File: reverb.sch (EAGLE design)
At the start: 70 parts, among them IC2 TL074, IC2_EQ1 NE5532, IC4_DRV_RCVR TL072, T1 2N3904

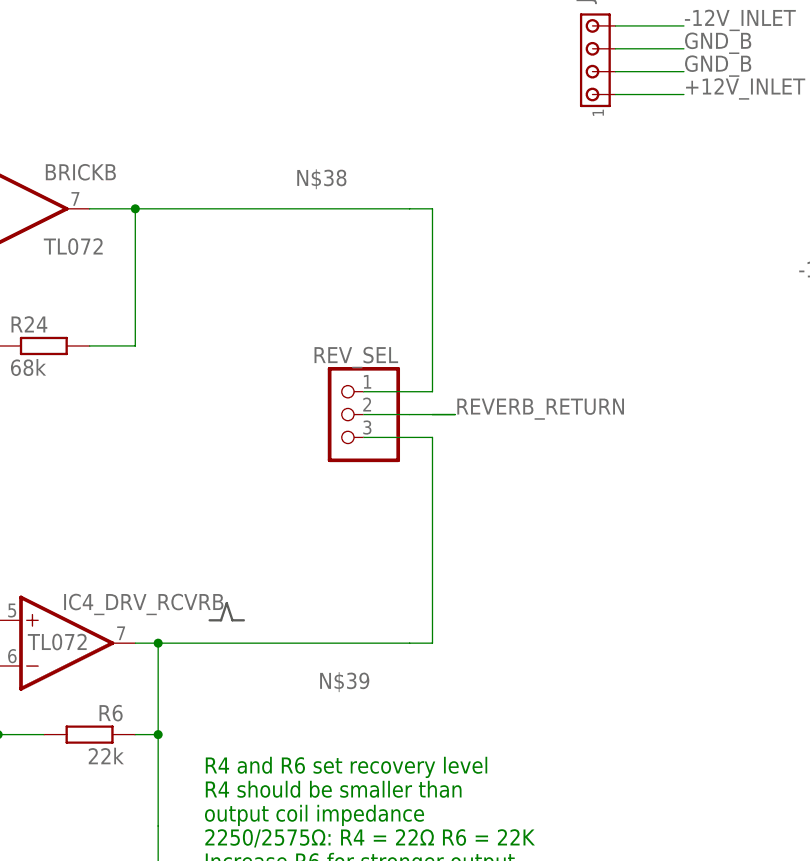
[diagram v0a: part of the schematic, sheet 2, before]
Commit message: fixed multiple power busses, ditched selection jumpers, layed out more board
selection jumpers: we're just gonna ditch part of the schematic anyways
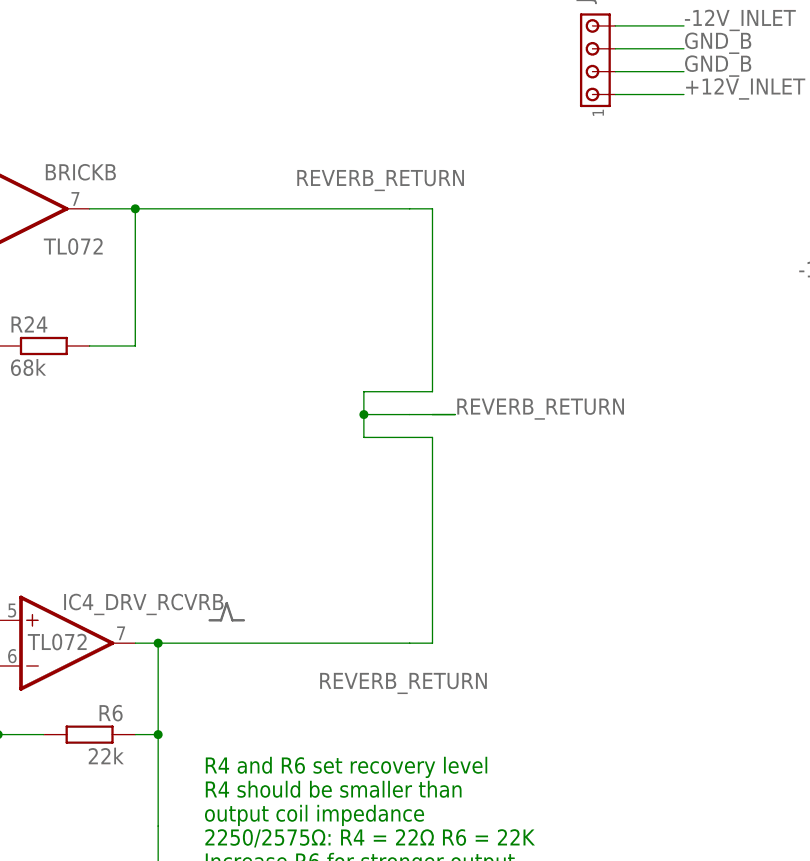
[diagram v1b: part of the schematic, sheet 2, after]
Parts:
- removed REV_SEL: (no value), pinhead:PINHD-1X3
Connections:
- removed net -12V: C11.1, C16.2
- removed net N$38: BRICKB.OUT, R24.2, REV_SEL.1
- removed net N$39: C9.2, IC4_DRV_RCVRB.OUT, R6.1, REV_SEL.3
- net +12V: no longer C10.2, C5.2
- net +12V_B: now also C10.2, C5.2
- net -12V_B: now also C11.1, C16.2
- net REVERB_RETURN: now also BRICKB.OUT, C9.2, IC4_DRV_RCVRB.OUT, R24.2, R6.1; no longer REV_SEL.2
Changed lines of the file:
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@@
 <part name="CV_IN" library="pinhead" deviceset="PINHD-1X2" device=""/>
 <part name="J1" library="con-amp" deviceset="MTA04-156" device=""/>
-<part name="REV_SEL" library="pinhead" deviceset="PINHD-1X3" device=""/>
 </parts>
 <sheets>
@@
 <label x="68.58" y="127" size="1.778" layer="95"/>
 </segment>
+<segment>
+<pinref part="C10" gate="G$1" pin="2"/>
+<wire x1="38.1" y1="88.9" x2="38.1" y2="86.36" width="0.1524" layer="91"/>
+<label x="38.1" y="88.9" size="1.778" layer="95"/>
+<pinref part="C5" gate="G$1" pin="2"/>
+<wire x1="50.8" y1="86.36" x2="38.1" y2="86.36" width="0.1524" layer="91"/>
+<junction x="38.1" y="86.36"/>
+</segment>
 </net>
 <net name="GND_B" class="2">
@@
 <label x="185.42" y="127" size="1.778" layer="95"/>
 </segment>
-</net>
-<net name="+12V" class="1">
-<segment>
-<pinref part="C10" gate="G$1" pin="2"/>
-<wire x1="38.1" y1="88.9" x2="38.1" y2="86.36" width="0.1524" layer="91"/>
-<label x="38.1" y="88.9" size="1.778" layer="95"/>
-<pinref part="C5" gate="G$1" pin="2"/>
-<wire x1="50.8" y1="86.36" x2="38.1" y2="86.36" width="0.1524" layer="91"/>
-<junction x="38.1" y="86.36"/>
-</segment>
-</net>
-<net name="-12V" class="1">
 <segment>
 <pinref part="C11" gate="G$1" pin="1"/>
@@
 <instance part="R2" gate="G$1" x="33.02" y="55.88"/>
 <instance part="J1" gate="G$3" x="205.74" y="157.48" rot="R90"/>
-<instance part="REV_SEL" gate="A" x="177.8" y="121.92" rot="MR0"/>
 </instances>
 <busses>
@@
 <label x="190.5" y="121.92" size="1.778" layer="95"/>
 <wire x1="190.5" y1="121.92" x2="187.96" y2="121.92" width="0.1524" layer="91"/>
-<pinref part="REV_SEL" gate="A" pin="2"/>
 <wire x1="187.96" y1="121.92" x2="185.42" y2="121.92" width="0.1524" layer="91"/>
 <wire x1="185.42" y1="121.92" x2="180.34" y2="121.92" width="0.1524" layer="91"/>
+<pinref part="BRICK" gate="B" pin="OUT"/>
+<wire x1="149.86" y1="144.78" x2="154.94" y2="144.78" width="0.1524" layer="91"/>
+<wire x1="154.94" y1="144.78" x2="185.42" y2="144.78" width="0.1524" layer="91"/>
+<pinref part="R24" gate="G$1" pin="2"/>
+<wire x1="149.86" y1="129.54" x2="154.94" y2="129.54" width="0.1524" layer="91"/>
+<wire x1="154.94" y1="129.54" x2="154.94" y2="144.78" width="0.1524" layer="91"/>
+<junction x="154.94" y="144.78"/>
+<label x="172.72" y="147.32" size="1.778" layer="95"/>
+<wire x1="185.42" y1="144.78" x2="187.96" y2="144.78" width="0.1524" layer="91"/>
+<wire x1="187.96" y1="144.78" x2="187.96" y2="124.46" width="0.1524" layer="91"/>
+<wire x1="187.96" y1="124.46" x2="180.34" y2="124.46" width="0.1524" layer="91"/>
+<wire x1="180.34" y1="124.46" x2="180.34" y2="121.92" width="0.1524" layer="91"/>
+<pinref part="R6" gate="G$1" pin="1"/>
+<wire x1="154.94" y1="86.36" x2="157.48" y2="86.36" width="0.1524" layer="91"/>
+<wire x1="157.48" y1="76.2" x2="157.48" y2="86.36" width="0.1524" layer="91"/>
+<wire x1="157.48" y1="63.5" x2="157.48" y2="76.2" width="0.1524" layer="91"/>
+<pinref part="C9" gate="G$1" pin="2"/>
+<wire x1="154.94" y1="63.5" x2="157.48" y2="63.5" width="0.1524" layer="91"/>
+<pinref part="IC4_DRV_RCVR" gate="B" pin="OUT"/>
+<wire x1="154.94" y1="96.52" x2="157.48" y2="96.52" width="0.1524" layer="91"/>
+<wire x1="157.48" y1="96.52" x2="185.42" y2="96.52" width="0.1524" layer="91"/>
+<wire x1="157.48" y1="86.36" x2="157.48" y2="96.52" width="0.1524" layer="91"/>
+<junction x="157.48" y="86.36"/>
+<junction x="157.48" y="96.52"/>
+<label x="175.26" y="91.44" size="1.778" layer="95"/>
+<wire x1="180.34" y1="119.38" x2="187.96" y2="119.38" width="0.1524" layer="91"/>
+<wire x1="187.96" y1="119.38" x2="187.96" y2="96.52" width="0.1524" layer="91"/>
+<wire x1="187.96" y1="96.52" x2="185.42" y2="96.52" width="0.1524" layer="91"/>
+<wire x1="180.34" y1="119.38" x2="180.34" y2="121.92" width="0.1524" layer="91"/>
+<junction x="180.34" y="121.92"/>
 </segment>
 </net>
@@
 </segment>
 </net>
-<net name="N$38" class="0">
-<segment>
-<pinref part="BRICK" gate="B" pin="OUT"/>
-<wire x1="149.86" y1="144.78" x2="154.94" y2="144.78" width="0.1524" layer="91"/>
-<wire x1="154.94" y1="144.78" x2="185.42" y2="144.78" width="0.1524" layer="91"/>
-<pinref part="R24" gate="G$1" pin="2"/>
-<wire x1="149.86" y1="129.54" x2="154.94" y2="129.54" width="0.1524" layer="91"/>
-<wire x1="154.94" y1="129.54" x2="154.94" y2="144.78" width="0.1524" layer="91"/>
-<junction x="154.94" y="144.78"/>
-<label x="172.72" y="147.32" size="1.778" layer="95"/>
-<wire x1="185.42" y1="144.78" x2="187.96" y2="144.78" width="0.1524" layer="91"/>
-<wire x1="187.96" y1="144.78" x2="187.96" y2="124.46" width="0.1524" layer="91"/>
-<pinref part="REV_SEL" gate="A" pin="1"/>
-<wire x1="187.96" y1="124.46" x2="180.34" y2="124.46" width="0.1524" layer="91"/>
-</segment>
-</net>
-<net name="N$39" class="0">
-<segment>
-<pinref part="R6" gate="G$1" pin="1"/>
-<wire x1="154.94" y1="86.36" x2="157.48" y2="86.36" width="0.1524" layer="91"/>
-<wire x1="157.48" y1="76.2" x2="157.48" y2="86.36" width="0.1524" layer="91"/>
-<wire x1="157.48" y1="63.5" x2="157.48" y2="76.2" width="0.1524" layer="91"/>
-<pinref part="C9" gate="G$1" pin="2"/>
-<wire x1="154.94" y1="63.5" x2="157.48" y2="63.5" width="0.1524" layer="91"/>
-<pinref part="IC4_DRV_RCVR" gate="B" pin="OUT"/>
-<wire x1="154.94" y1="96.52" x2="157.48" y2="96.52" width="0.1524" layer="91"/>
-<wire x1="157.48" y1="96.52" x2="185.42" y2="96.52" width="0.1524" layer="91"/>
-<wire x1="157.48" y1="86.36" x2="157.48" y2="96.52" width="0.1524" layer="91"/>
-<junction x="157.48" y="86.36"/>
-<junction x="157.48" y="96.52"/>
-<label x="175.26" y="91.44" size="1.778" layer="95"/>
-<pinref part="REV_SEL" gate="A" pin="3"/>
-<wire x1="180.34" y1="119.38" x2="187.96" y2="119.38" width="0.1524" layer="91"/>
-<wire x1="187.96" y1="119.38" x2="187.96" y2="96.52" width="0.1524" layer="91"/>
-<wire x1="187.96" y1="96.52" x2="185.42" y2="96.52" width="0.1524" layer="91"/>
-</segment>
-</net>

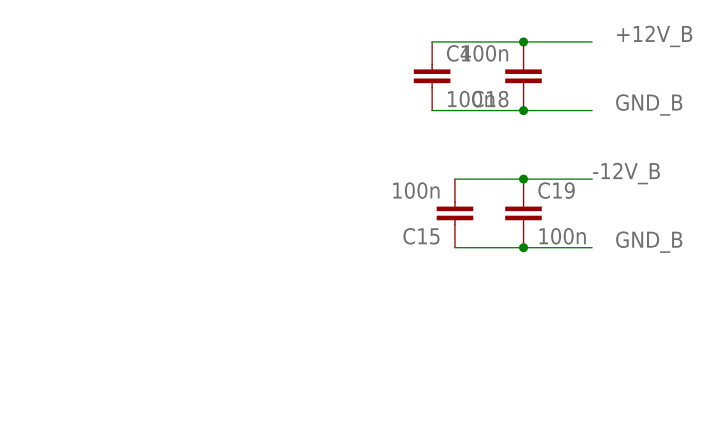
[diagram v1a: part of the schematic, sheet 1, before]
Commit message: everything should be on the board, just need to move it around
gonna ditch brick section soon, detached it
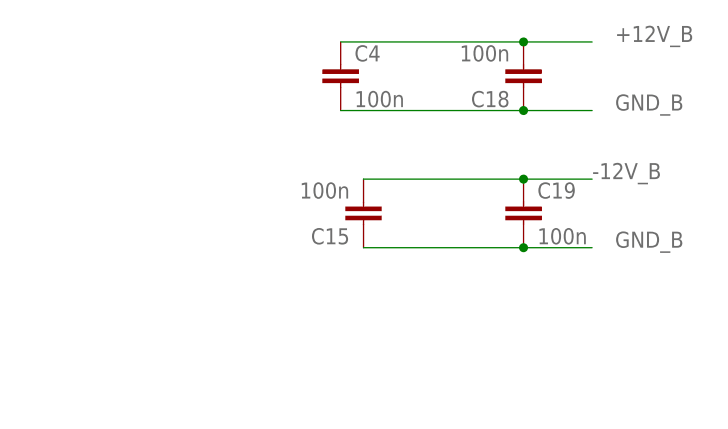
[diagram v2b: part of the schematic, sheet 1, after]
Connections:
- new net BRICKREVERB_SEND: R22.1
- new net BRICK_REVERB_RETURN: BRICKB.OUT, R24.2
- net REVERB_RETURN: no longer BRICKB.OUT, R24.2
- net REVERB_SEND: no longer R22.1
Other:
- moved on the sheet: C15, C4
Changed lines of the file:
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@@
 <instance part="FRAME2" gate="G$2" x="162.56" y="0"/>
 <instance part="IC4_DRV_RCVR" gate="P" x="170.18" y="81.28"/>
-<instance part="C4" gate="G$1" x="167.64" y="139.7"/>
-<instance part="C15" gate="G$1" x="170.18" y="121.92" rot="R180"/>
+<instance part="C4" gate="G$1" x="157.48" y="139.7"/>
+<instance part="C15" gate="G$1" x="160.02" y="121.92" rot="R180"/>
 <instance part="C14" gate="G$1" x="81.28" y="124.46"/>
 <instance part="C17" gate="G$1" x="81.28" y="109.22"/>
@@
 <label x="187.96" y="142.24" size="1.778" layer="95"/>
 <pinref part="C18" gate="G$1" pin="2"/>
-<wire x1="177.8" y1="142.24" x2="167.64" y2="142.24" width="0.1524" layer="91"/>
+<wire x1="177.8" y1="142.24" x2="157.48" y2="142.24" width="0.1524" layer="91"/>
 <junction x="177.8" y="142.24"/>
 </segment>
@@
 <label x="187.96" y="134.62" size="1.778" layer="95"/>
 <pinref part="C18" gate="G$1" pin="1"/>
-<wire x1="177.8" y1="134.62" x2="167.64" y2="134.62" width="0.1524" layer="91"/>
+<wire x1="177.8" y1="134.62" x2="157.48" y2="134.62" width="0.1524" layer="91"/>
 <junction x="177.8" y="134.62"/>
 </segment>
@@
 <label x="187.96" y="119.38" size="1.778" layer="95"/>
 <pinref part="C19" gate="G$1" pin="2"/>
-<wire x1="177.8" y1="119.38" x2="170.18" y2="119.38" width="0.1524" layer="91"/>
+<wire x1="177.8" y1="119.38" x2="160.02" y2="119.38" width="0.1524" layer="91"/>
 <junction x="177.8" y="119.38"/>
 </segment>
@@
 <wire x1="185.42" y1="127" x2="177.8" y2="127" width="0.1524" layer="91"/>
 <pinref part="C15" gate="G$1" pin="2"/>
-<wire x1="177.8" y1="127" x2="170.18" y2="127" width="0.1524" layer="91"/>
+<wire x1="177.8" y1="127" x2="160.02" y2="127" width="0.1524" layer="91"/>
 <junction x="177.8" y="127"/>
 <label x="185.42" y="127" size="1.778" layer="95"/>
@@
 <wire x1="187.96" y1="121.92" x2="185.42" y2="121.92" width="0.1524" layer="91"/>
 <wire x1="185.42" y1="121.92" x2="180.34" y2="121.92" width="0.1524" layer="91"/>
-<pinref part="BRICK" gate="B" pin="OUT"/>
-<wire x1="149.86" y1="144.78" x2="154.94" y2="144.78" width="0.1524" layer="91"/>
-<wire x1="154.94" y1="144.78" x2="185.42" y2="144.78" width="0.1524" layer="91"/>
-<pinref part="R24" gate="G$1" pin="2"/>
-<wire x1="149.86" y1="129.54" x2="154.94" y2="129.54" width="0.1524" layer="91"/>
-<wire x1="154.94" y1="129.54" x2="154.94" y2="144.78" width="0.1524" layer="91"/>
-<junction x="154.94" y="144.78"/>
-<label x="172.72" y="147.32" size="1.778" layer="95"/>
-<wire x1="185.42" y1="144.78" x2="187.96" y2="144.78" width="0.1524" layer="91"/>
-<wire x1="187.96" y1="144.78" x2="187.96" y2="124.46" width="0.1524" layer="91"/>
-<wire x1="187.96" y1="124.46" x2="180.34" y2="124.46" width="0.1524" layer="91"/>
 <wire x1="180.34" y1="124.46" x2="180.34" y2="121.92" width="0.1524" layer="91"/>
 <pinref part="R6" gate="G$1" pin="1"/>
@@
 <wire x1="38.1" y1="101.6" x2="40.64" y2="101.6" width="0.1524" layer="91"/>
 </segment>
-<segment>
-<wire x1="33.02" y1="162.56" x2="48.26" y2="162.56" width="0.1524" layer="91"/>
-<label x="25.4" y="162.56" size="1.778" layer="95"/>
-<pinref part="R22" gate="G$1" pin="1"/>
-</segment>
 </net>
 <net name="N$19" class="0">
@@
 </segment>
 </net>
+<net name="BRICK_REVERB_RETURN" class="0">
+<segment>
+<wire x1="185.42" y1="144.78" x2="187.96" y2="144.78" width="0.1524" layer="91"/>
+<pinref part="BRICK" gate="B" pin="OUT"/>
+<wire x1="149.86" y1="144.78" x2="154.94" y2="144.78" width="0.1524" layer="91"/>
+<wire x1="154.94" y1="144.78" x2="185.42" y2="144.78" width="0.1524" layer="91"/>
+<junction x="154.94" y="144.78"/>
+<wire x1="154.94" y1="129.54" x2="154.94" y2="144.78" width="0.1524" layer="91"/>
+<pinref part="R24" gate="G$1" pin="2"/>
+<wire x1="149.86" y1="129.54" x2="154.94" y2="129.54" width="0.1524" layer="91"/>
+<label x="172.72" y="147.32" size="1.778" layer="95"/>
+</segment>
+</net>
+<net name="BRICKREVERB_SEND" class="0">
+<segment>
+<wire x1="33.02" y1="162.56" x2="48.26" y2="162.56" width="0.1524" layer="91"/>
+<label x="25.4" y="162.56" size="1.778" layer="95"/>
+<pinref part="R22" gate="G$1" pin="1"/>
+</segment>
+</net>

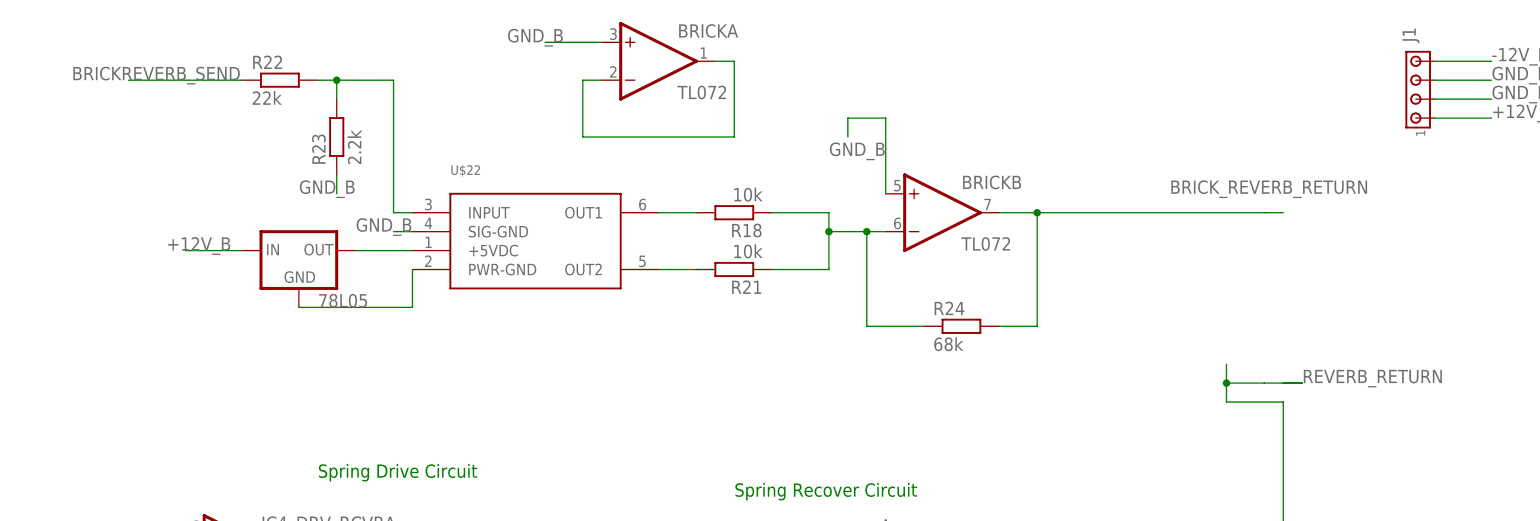
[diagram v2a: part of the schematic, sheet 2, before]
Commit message: ditched brick section
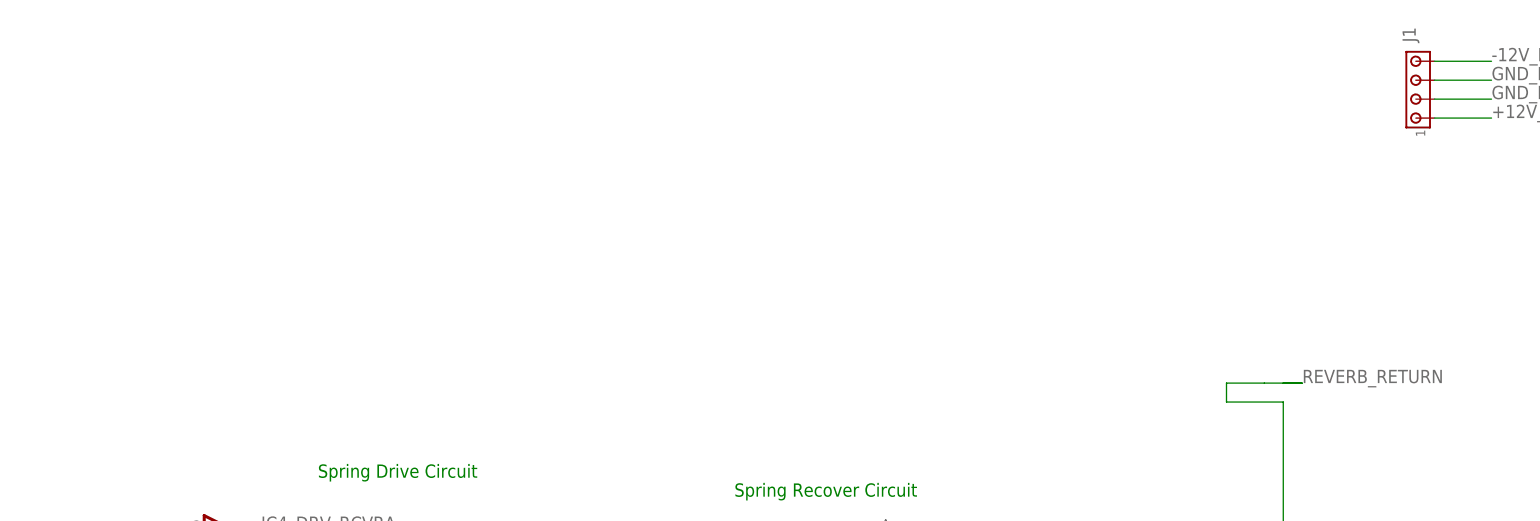
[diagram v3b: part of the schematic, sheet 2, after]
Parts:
- removed 78L05: (no value), SparkFun-PowerIC:V_REG_78XXTO-92
- removed BRICK: TL072, TomW:TL072P
- removed C18, C19: 100n, TomW:C-EU050-024X044
- removed R18, R21: 10k, TomW:R-EU_STANDARD_RESISTOR
- removed R22: 22k, TomW:R-EU_STANDARD_RESISTOR
- removed R23: 2.2k, TomW:R-EU_STANDARD_RESISTOR
- removed R24: 68k, TomW:R-EU_STANDARD_RESISTOR
- removed U$22: (no value), Accutronics BTDR-2H:BTDR-2H
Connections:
- removed net BRICKREVERB_SEND: R22.1
- removed net BRICK_REVERB_RETURN: BRICKB.OUT, R24.2
- removed net N$19: 78L05.OUT, U$22.+5VDC
- removed net N$27: R22.2, R23.2, U$22.INPUT
- removed net N$28: R18.2, U$22.OUT1
- removed net N$29: R21.2, U$22.OUT2
- removed net N$30: BRICKB.-IN, R18.1, R21.1, R24.1
- removed net N$32: 78L05.GND, U$22.PWR-GND
- removed net N$34: BRICKA.-IN, BRICKA.OUT
- net +12V_B: no longer 78L05.IN, BRICKP.V+, C18.2
- net -12V_B: no longer BRICKP.V-, C19.1
- net GND_B: no longer BRICKA.+IN, BRICKB.+IN, C18.1, C19.2, R23.1, U$22.SIG-GND

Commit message: almost layed out, almost ready for routing!
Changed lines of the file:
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@@
 <net name="REVERB_RETURN" class="0">
 <segment>
-<wire x1="187.96" y1="121.92" x2="190.5" y2="121.92" width="0.1524" layer="91"/>
-<label x="190.5" y="121.92" size="1.778" layer="95"/>
-<wire x1="190.5" y1="121.92" x2="187.96" y2="121.92" width="0.1524" layer="91"/>
-<wire x1="187.96" y1="121.92" x2="185.42" y2="121.92" width="0.1524" layer="91"/>
-<wire x1="185.42" y1="121.92" x2="180.34" y2="121.92" width="0.1524" layer="91"/>
 <pinref part="R6" gate="G$1" pin="1"/>
 <wire x1="154.94" y1="86.36" x2="157.48" y2="86.36" width="0.1524" layer="91"/>
@@
 <junction x="157.48" y="96.52"/>
 <label x="175.26" y="91.44" size="1.778" layer="95"/>
-<wire x1="180.34" y1="119.38" x2="187.96" y2="119.38" width="0.1524" layer="91"/>
-<wire x1="187.96" y1="119.38" x2="187.96" y2="96.52" width="0.1524" layer="91"/>
 <wire x1="187.96" y1="96.52" x2="185.42" y2="96.52" width="0.1524" layer="91"/>
-<wire x1="180.34" y1="119.38" x2="180.34" y2="121.92" width="0.1524" layer="91"/>
 </segment>
 </net>

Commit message: oops, grounds weren't connected..
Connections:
- removed net GND_B: C14.-, C15.1, C17.+, C4.2, D3.C, D4.A, J1.2, J1.3, R2.E, R2.S, R4.2, R5.1, TO_OUTPUT.2
- net GND: now also C14.-, C15.1, C17.+, C4.2, D3.C, D4.A, J1.2, J1.3, R2.E, R2.S, R4.2, R5.1, TO_OUTPUT.2
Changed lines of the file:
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@@
-</segment>
-</net>
-<net name="GND_B" class="2">
-<segment>
-<pinref part="C4" gate="G$1" pin="2"/>
-<wire x1="185.42" y1="134.62" x2="177.8" y2="134.62" width="0.1524" layer="91"/>
-<label x="187.96" y="134.62" size="1.778" layer="95"/>
-<wire x1="177.8" y1="134.62" x2="157.48" y2="134.62" width="0.1524" layer="91"/>
-</segment>
-<segment>
-<pinref part="C15" gate="G$1" pin="1"/>
-<wire x1="185.42" y1="119.38" x2="177.8" y2="119.38" width="0.1524" layer="91"/>
-<label x="187.96" y="119.38" size="1.778" layer="95"/>
-<wire x1="177.8" y1="119.38" x2="160.02" y2="119.38" width="0.1524" layer="91"/>
-</segment>
-<segment>
-<pinref part="C14" gate="G$1" pin="-"/>
-<wire x1="81.28" y1="111.76" x2="81.28" y2="114.3" width="0.1524" layer="91"/>
-<pinref part="C17" gate="G$1" pin="+"/>
-<wire x1="81.28" y1="114.3" x2="81.28" y2="119.38" width="0.1524" layer="91"/>
-<wire x1="81.28" y1="114.3" x2="99.06" y2="114.3" width="0.1524" layer="91"/>
-<junction x="81.28" y="114.3"/>
-<label x="93.98" y="114.3" size="1.778" layer="95"/>
 </segment>
 </net>
@@
 <wire x1="50.8" y1="76.2" x2="38.1" y2="76.2" width="0.1524" layer="91"/>
 <junction x="38.1" y="76.2"/>
+</segment>
+<segment>
+<pinref part="C4" gate="G$1" pin="2"/>
+<wire x1="185.42" y1="134.62" x2="177.8" y2="134.62" width="0.1524" layer="91"/>
+<label x="187.96" y="134.62" size="1.778" layer="95"/>
+<wire x1="177.8" y1="134.62" x2="157.48" y2="134.62" width="0.1524" layer="91"/>
+</segment>
+<segment>
+<pinref part="C15" gate="G$1" pin="1"/>
+<wire x1="185.42" y1="119.38" x2="177.8" y2="119.38" width="0.1524" layer="91"/>
+<label x="187.96" y="119.38" size="1.778" layer="95"/>
+<wire x1="177.8" y1="119.38" x2="160.02" y2="119.38" width="0.1524" layer="91"/>
+</segment>
+<segment>
+<pinref part="C14" gate="G$1" pin="-"/>
+<wire x1="81.28" y1="111.76" x2="81.28" y2="114.3" width="0.1524" layer="91"/>
+<pinref part="C17" gate="G$1" pin="+"/>
+<wire x1="81.28" y1="114.3" x2="81.28" y2="119.38" width="0.1524" layer="91"/>
+<wire x1="81.28" y1="114.3" x2="99.06" y2="114.3" width="0.1524" layer="91"/>
+<junction x="81.28" y="114.3"/>
+<label x="93.98" y="114.3" size="1.778" layer="95"/>
 </segment>
 </net>
@@
 </busses>
 <nets>
-<net name="GND_B" class="2">
+<net name="GND" class="2">
 <segment>
 <pinref part="SUPPLY4" gate="GND" pin="GND"/>
